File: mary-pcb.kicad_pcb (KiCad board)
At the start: 2 copper layers, 69 parts, among them SW1 SW_Push, SW2 Rotary_Encoder_Switch, U1 ATmega32U4-AU, Y1 16MHz

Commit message: place switches on pcb
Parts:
- moved MX20 236.5 mm to (257.2, 114.3)
- moved MX26 235.3 mm to (257.2, 123.8), turned to 90 degrees
- moved MX16 230.2 mm to (257.2, 85.7), turned to 90 degrees
- moved MX25 216.6 mm to (257.2, 133.3)
- moved MX23 199.1 mm to (219.1, 133.3)
- moved MX24 176.6 mm to (238.1, 133.3)
- moved MX3 175.1 mm to (238.1, 33.3)
- moved MX21 173.2 mm to (209.6, 133.3)
- moved MX15 171.3 mm to (257.2, 95.2)
- moved MX22 168.2 mm to (200.0, 133.3)
- moved MX6 152.2 mm to (238.1, 57.1)
- moved MX1 135.7 mm to (200.0, 33.3)
- moved MX14 135.2 mm to (238.1, 95.2)
- moved MX19 134.9 mm to (238.1, 114.3)
- moved MX8 134.4 mm to (200.0, 76.2)
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
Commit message: tentative rotary encoder placement
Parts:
- moved SW2 121.4 mm to (257.2, 33.3)
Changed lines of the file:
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@@
   )
   (module Keebio-Parts:RotaryEncoder_EC11 (layer F.Cu)
-    (at 146.2075 82.59125)
+    (at 257.175 33.3375)
     (descr "Alps rotary encoder, EC12E... with switch, vertical shaft, http://www.alps.com/prod/info/E/HTML/Encoder/Incremental/EC11/EC11E15204A3.html")
     (tags "rotary encoder")

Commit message: fix switch placement
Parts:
- moved MX1 4.76 mm to (200.0, 28.6)
- moved MX2 4.76 mm to (219.1, 28.6)
- moved MX3 4.76 mm to (238.1, 28.6)
- moved SW2 4.76 mm to (257.2, 28.6), turned to 90 degrees
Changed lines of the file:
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@@
   )
   (module Keebio-Parts:RotaryEncoder_EC11 (layer F.Cu)
-    (at 257.175 33.3375)
+    (at 257.175 28.575 90)
     (descr "Alps rotary encoder, EC12E... with switch, vertical shaft, http://www.alps.com/prod/info/E/HTML/Encoder/Incremental/EC11/EC11E15204A3.html")
     (tags "rotary encoder")
-    (fp_text reference SW2 (at -4.7 -7.2) (layer F.Fab)
-      (effects (font (size 1 1) (thickness 0.15)))
-    )
-    (fp_text value Rotary_Encoder_Switch (at 0 7.9) (layer F.Fab)
-      (effects (font (size 1 1) (thickness 0.15)))
-    )
-    (fp_text user %R (at 3.6 3.8) (layer F.Fab)
+    (fp_text reference SW2 (at -4.7 -7.2 90) (layer F.Fab)
+      (effects (font (size 1 1) (thickness 0.15)))
+    )
+    (fp_text value Rotary_Encoder_Switch (at 0 7.9 90) (layer F.Fab)
+      (effects (font (size 1 1) (thickness 0.15)))
+    )
+    (fp_text user %R (at 3.6 3.8 90) (layer F.Fab)
       (effects (font (size 1 1) (thickness 0.15)))
     )
@@
     (fp_circle (center 0 0) (end 3 0) (layer F.SilkS) (width 0.12))
     (fp_circle (center 0 0) (end 3 0) (layer F.Fab) (width 0.12))
-    (pad A thru_hole rect (at -7.5 -2.5) (size 2 2) (drill 1) (layers *.Cu *.Mask)
+    (pad A thru_hole rect (at -7.5 -2.5 90) (size 2 2) (drill 1) (layers *.Cu *.Mask)
       (net 49 "A(Left?)"))
-    (pad C thru_hole circle (at -7.5 0) (size 2 2) (drill 1) (layers *.Cu *.Mask)
+    (pad C thru_hole circle (at -7.5 0 90) (size 2 2) (drill 1) (layers *.Cu *.Mask)
       (net 1 GND))
-    (pad B thru_hole circle (at -7.5 2.5) (size 2 2) (drill 1) (layers *.Cu *.Mask)
+    (pad B thru_hole circle (at -7.5 2.5 90) (size 2 2) (drill 1) (layers *.Cu *.Mask)
       (net 50 "B(Right?)"))
-    (pad "" np_thru_hole rect (at 0 -5.6) (size 3.2 2) (drill oval 2.8 1.5) (layers *.Cu *.Mask))
-    (pad "" np_thru_hole rect (at 0 5.6) (size 3.2 2) (drill oval 2.8 1.5) (layers *.Cu *.Mask))
-    (pad S2 thru_hole circle (at 7 -2.5) (size 2 2) (drill 1) (layers *.Cu *.Mask)
+    (pad "" np_thru_hole rect (at 0 -5.6 90) (size 3.2 2) (drill oval 2.8 1.5) (layers *.Cu *.Mask))
+    (pad "" np_thru_hole rect (at 0 5.6 90) (size 3.2 2) (drill oval 2.8 1.5) (layers *.Cu *.Mask))
+    (pad S2 thru_hole circle (at 7 -2.5 90) (size 2 2) (drill 1) (layers *.Cu *.Mask)
       (net 10 "Net-(D4-Pad2)"))
-    (pad S1 thru_hole circle (at 7 2.5) (size 2 2) (drill 1) (layers *.Cu *.Mask)
+    (pad S1 thru_hole circle (at 7 2.5 90) (size 2 2) (drill 1) (layers *.Cu *.Mask)
       (net 40 Col3))
     (model ${KISYS3DMOD}/Rotary_Encoder.3dshapes/RotaryEncoder_Alps_EC11E-Switch_Vertical_H20mm.wrl
@@
   )
   (module MX_Alps_Hybrid:MX-1U-NoLED (layer F.Cu)
-    (at 238.125 33.3375)
+    (at 238.125 28.575)
     (fp_text reference MX3 (at 0 3.175) (layer Dwgs.User)
       (effects (font (size 1 1) (thickness 0.15)))
@@
   )
   (module MX_Alps_Hybrid:MX-1U-NoLED (layer F.Cu)
-    (at 219.075 33.3375)
+    (at 219.075 28.575)
     (fp_text reference MX2 (at 0 3.175) (layer Dwgs.User)
       (effects (font (size 1 1) (thickness 0.15)))
@@
   )
   (module MX_Alps_Hybrid:MX-1U-NoLED (layer F.Cu)
-    (at 200.025 33.3375)
+    (at 200.025 28.575)
     (fp_text reference MX1 (at 0 3.175) (layer Dwgs.User)
       (effects (font (size 1 1) (thickness 0.15)))

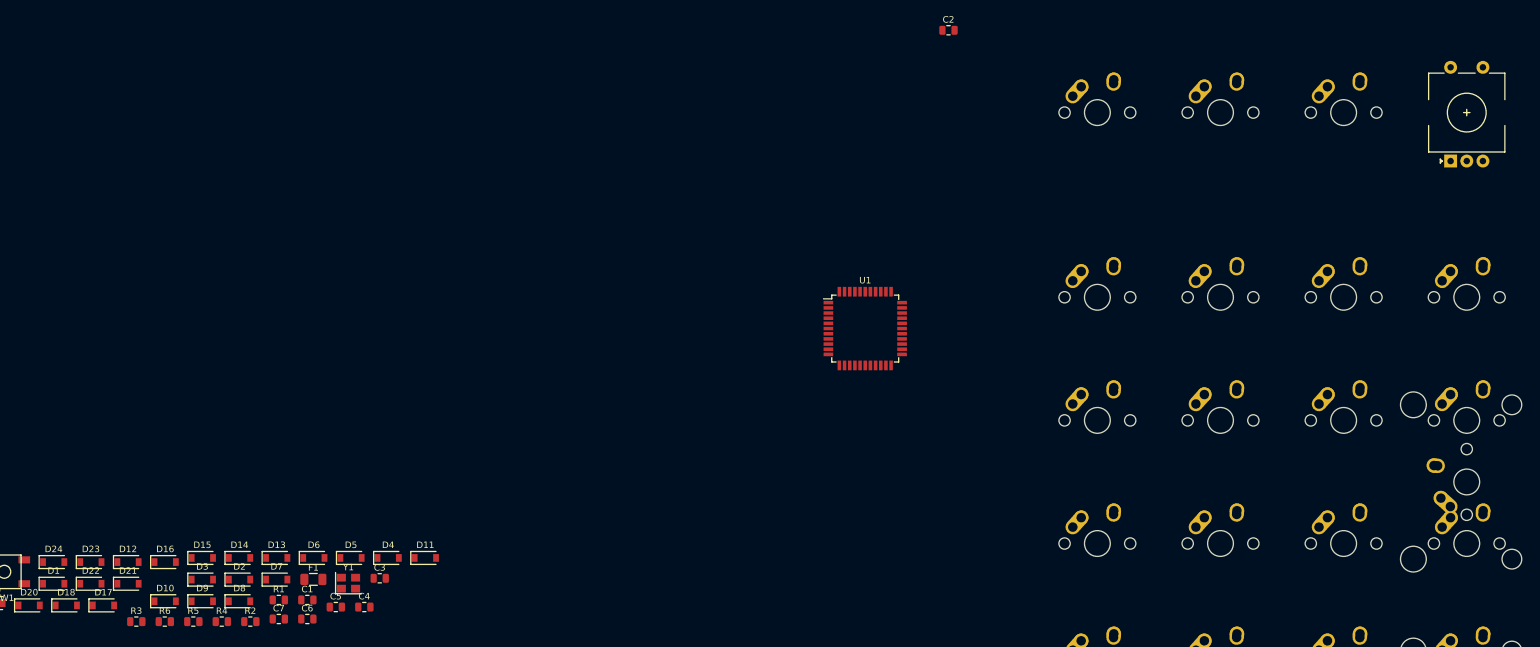
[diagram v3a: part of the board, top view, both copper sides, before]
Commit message: update pcb footprints, place diodes
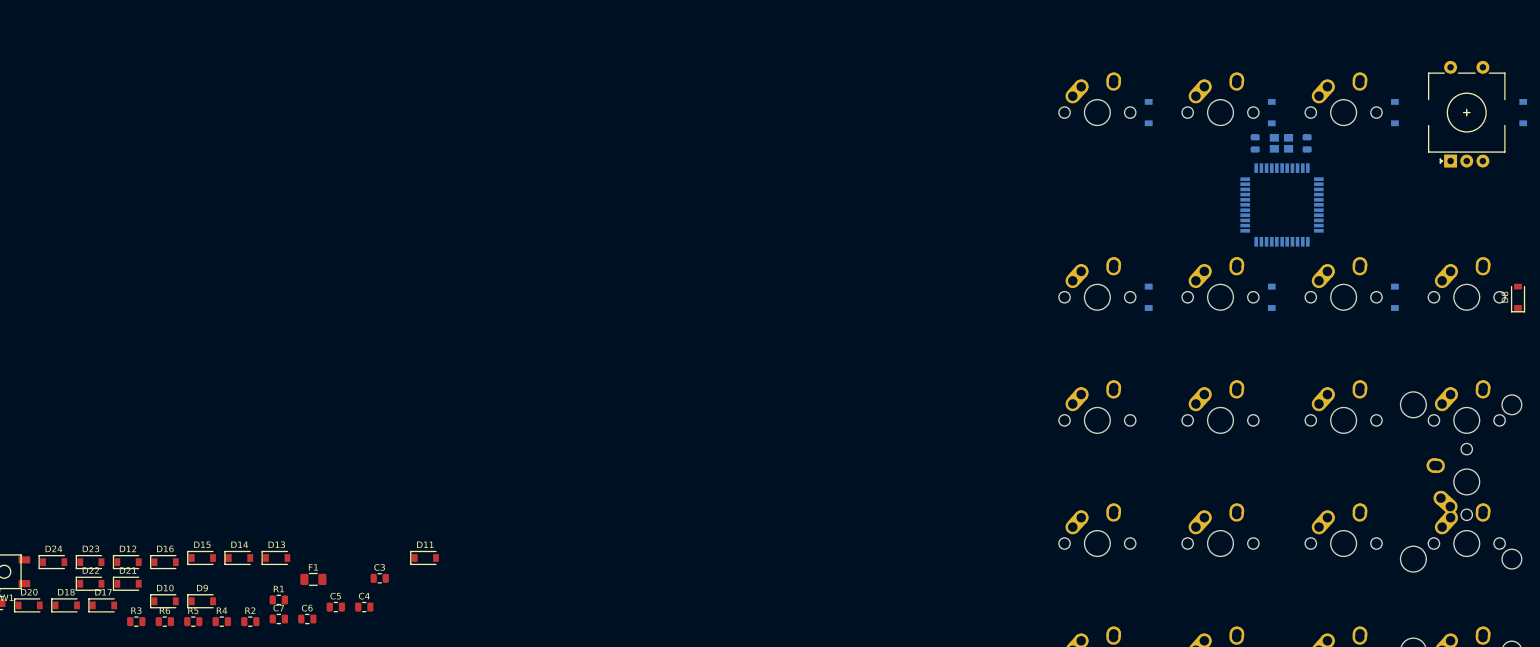
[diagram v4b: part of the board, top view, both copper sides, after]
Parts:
- C1, C2, D1, D2, D3, D4, D5, D6, D7, U1, Y1: moved to B.Cu
- moved D8 203.3 mm to (265.1, 57.1), turned to 90 degrees
- moved D3 198.2 mm to (246.1, 28.6), turned to 90 degrees
- moved D4 188.6 mm to (265.9, 28.6), turned to 90 degrees
- moved D1 184.4 mm to (208.0, 28.6), turned to 90 degrees
- moved D7 178.4 mm to (246.1, 57.1), turned to 90 degrees
- moved D2 175.3 mm to (227.0, 28.6), turned to 90 degrees
- moved C1 170.1 mm to (232.5, 33.3), turned to 90 degrees
- moved Y1 159.6 mm to (228.5, 33.3), turned to 180 degrees
- moved D6 153.6 mm to (227.0, 57.1), turned to 90 degrees
- moved D5 129.8 mm to (208.0, 57.1), turned to 90 degrees
- moved U1 67.3 mm to (228.6, 42.9)
- moved C2 50.6 mm to (224.4, 33.3), turned to 270 degrees
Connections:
- U1 pad 18: Row5 -> Net-(U1-Pad18)
- U1 pad 19: Col0 -> Net-(U1-Pad19)
- U1 pad 20: Col1 -> Net-(U1-Pad20)
- U1 pad 21: Col2 -> Net-(U1-Pad21)
- U1 pad 22: A(Left?) -> Net-(U1-Pad22)
- U1 pad 25: Col3 -> Net-(U1-Pad25)
- U1 pad 26: B(Right?) -> Net-(U1-Pad26)
- U1 pad 28: Row0 -> Net-(U1-Pad28)
- U1 pad 29: Row1 -> Net-(U1-Pad29)
- U1 pad 30: Row2 -> Net-(U1-Pad30)
- U1 pad 31: Row3 -> Net-(U1-Pad31)
- U1 pad 32: Row4 -> Net-(U1-Pad32)

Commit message: place resistors, diodes, reset, capacitors
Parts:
- C3, C4, C5, C6, C7, D10, D11, D12, D13, D14, D15, D16, D17, D18, D19, D20, D21, D22, D23, D24, D8, D9, F1, R1, R2, R3, R4, R5, R6, USB1: moved to B.Cu
- moved D20 156.6 mm to (188.9, 132.6), turned to 90 degrees
- moved D24 156.4 mm to (184.9, 153.2)
- moved USB1 151.9 mm to (153.2, 30.9)
- moved D19 146.0 mm to (172.2, 132.6), turned to 90 degrees
- moved D12 138.9 mm to (188.9, 94.5), turned to 90 degrees
- moved D23 135.7 mm to (168.3, 153.2)
- moved D16 134.5 mm to (188.9, 117.5), turned to 90 degrees
- moved D22 120.6 mm to (153.2, 153.2)
- moved D18 116.1 mm to (153.2, 132.6), turned to 90 degrees
- moved R6 115.8 mm to (161.9, 61.2), turned to 90 degrees
- moved R5 112.6 mm to (151.9, 42.0), turned to 90 degrees
- moved D15 112.5 mm to (172.2, 117.5), turned to 90 degrees
- moved R4 111.1 mm to (154.4, 42.0), turned to 90 degrees
- moved R3 110.1 mm to (135.4, 36.2), turned to 90 degrees
- moved SW1 103.2 mm to (124.6, 56.4)
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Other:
- board outline added: 76.2 x 123.8 mm

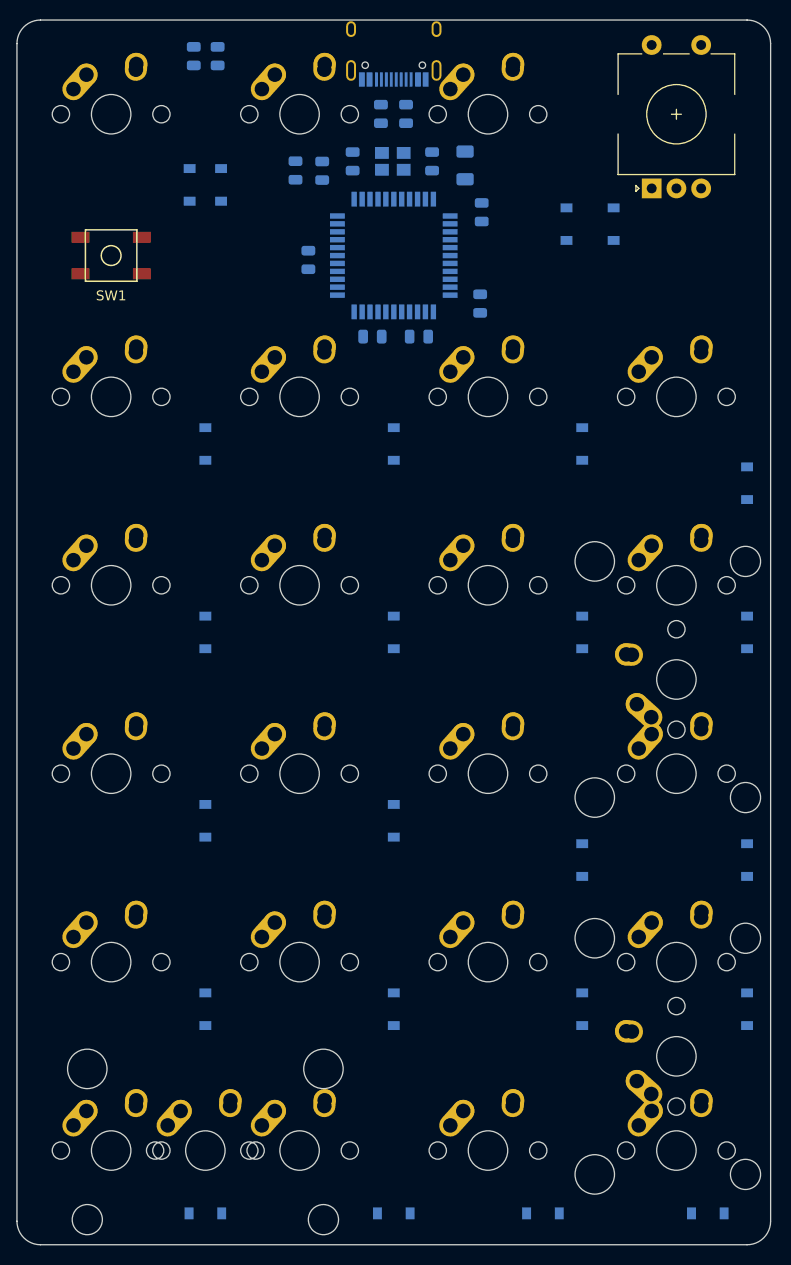
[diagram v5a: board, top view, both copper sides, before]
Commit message: complete routing
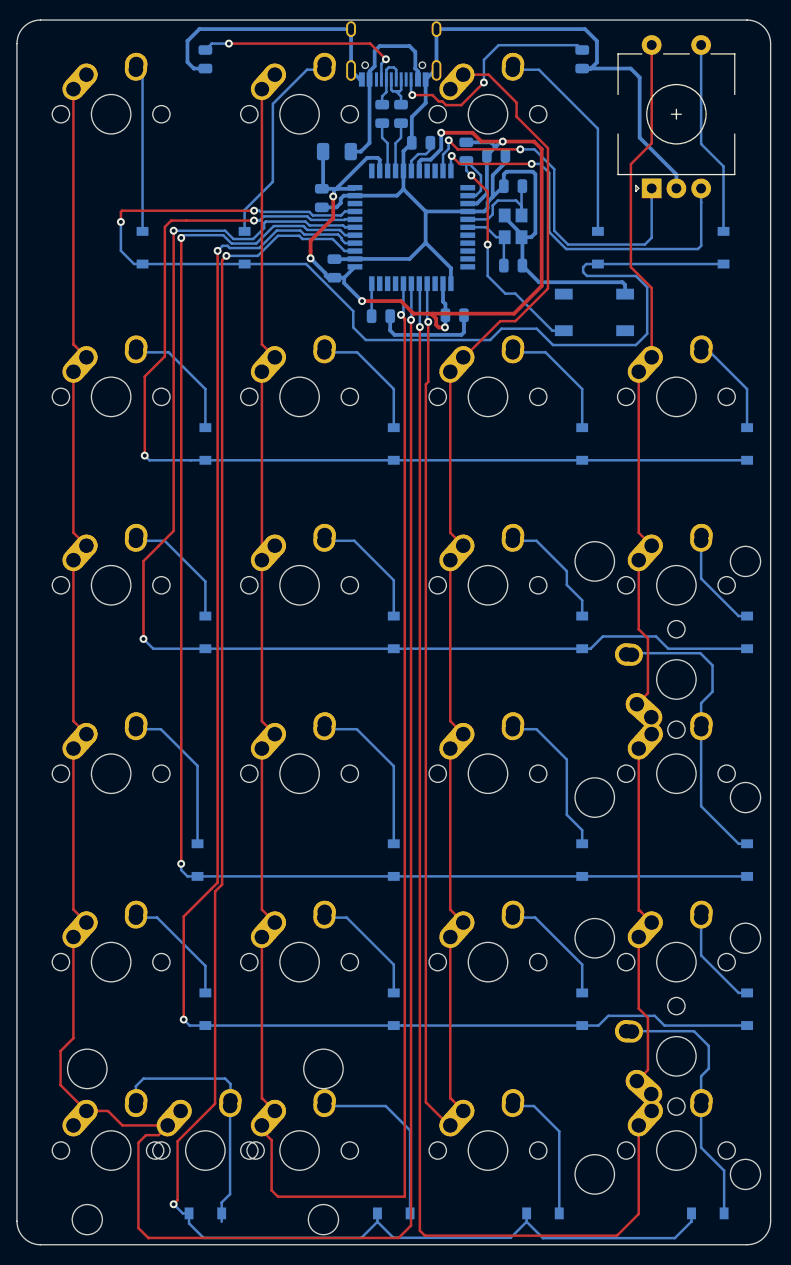
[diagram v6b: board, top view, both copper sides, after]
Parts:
- SW1: moved to B.Cu
- moved SW1 49.2 mm to (173.5, 62.1)
- moved R3 36.9 mm to (172.2, 36.5)
- moved C5 17.7 mm to (163.5, 46.3), turned to 0 degrees
- moved R1 17.4 mm to (160.5, 45.8)
- moved C3 16.4 mm to (156.0, 45.0), turned to 180 degrees
- moved C2 16.4 mm to (165.3, 49.3), turned to 180 degrees
- moved C7 14.9 mm to (145.9, 50.5), turned to 270 degrees
- moved Y1 13.8 mm to (165.3, 53.4), turned to 90 degrees
- moved C1 13.3 mm to (165.3, 57.4), turned to 0 degrees
- moved F1 13.0 mm to (147.4, 45.8), turned to 0 degrees
- moved D4 11.4 mm to (186.5, 55.6)
- moved C4 11.0 mm to (147.2, 57.7), turned to 90 degrees
- moved C6 10.8 mm to (159.4, 62.4), turned to 0 degrees
- moved R6 10.1 mm to (151.9, 62.5), turned to 180 degrees
- moved D1 7.94 mm to (127.8, 55.6)
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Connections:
- SW2 pad S1: Col3 -> Net-(D4-Pad2)
- SW2 pad S2: Net-(D4-Pad2) -> Col3
- U1 pad 10: Net-(U1-Pad10) -> A(Left?)
- U1 pad 11: Net-(U1-Pad11) -> B(Right?)
- U1 pad 26: Net-(U1-Pad26) -> Col2
- U1 pad 27: Net-(U1-Pad27) -> Col3
- U1 pad 28: Net-(U1-Pad28) -> Col0
- U1 pad 29: Net-(U1-Pad29) -> Col1
- U1 pad 36: Net-(U1-Pad36) -> Row5
- U1 pad 37: Net-(U1-Pad37) -> Row4
- U1 pad 38: Net-(U1-Pad38) -> Row3
- U1 pad 39: Net-(U1-Pad39) -> Row2
- U1 pad 40: Net-(U1-Pad40) -> Row1
- U1 pad 41: Net-(U1-Pad41) -> Row0
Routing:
- net Col0: track 0.00 -> 246.5 mm, vias 0 -> 1
- net Col3: track 0.00 -> 228.4 mm, vias 0 -> 1
- net Col1: track 0.00 -> 214.6 mm, vias 0 -> 1
- net Col2: track 0.00 -> 200.0 mm, vias 0 -> 1
- net Row5: track 0.00 -> 172.9 mm, vias 0 -> 2
- net GND: track 0.00 -> 169.9 mm
- net Row4: track 0.00 -> 152.7 mm, vias 0 -> 2
- net Row3: track 0.00 -> 140.5 mm, vias 0 -> 2
- net Row2: track 0.00 -> 124.9 mm, vias 0 -> 2
- net Row0: track 0.00 -> 114.2 mm, vias 0 -> 2
- net Row1: track 0.00 -> 104.9 mm, vias 0 -> 2
- net +5V: track 0.00 -> 99.6 mm, vias 0 -> 6
- net B(Right?): track 0.00 -> 40.1 mm, vias 0 -> 2
- net A(Left?): track 0.00 -> 37.1 mm, vias 0 -> 2
- net Net-(D16-Pad2): track 0.00 -> 29.7 mm
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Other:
- net class Default: trace_width 0.25 -> 0.254
- net class power added: clearance 0.2, trace_width 0.381, via_dia 0.8, via_drill 0.4

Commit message: complete routing, upload renders
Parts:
- moved SW1 11.3 mm to (182.9, 55.9)
- moved D3 4.72 mm to (170.7, 59.1)
- moved D2 4.23 mm to (135.7, 59.1)
- moved D4 4.23 mm to (188.9, 59.1)
- moved D1 3.49 mm to (127.8, 59.1)
- moved C5 3.46 mm to (167.0, 46.1)
- moved D21 3.13 mm to (136.8, 151.5), turned to 90 degrees
- moved C4 2.41 mm to (144.8, 57.7)
- moved D23 2.27 mm to (169.8, 151.5), turned to 90 degrees
- moved D22 1.69 mm to (153.0, 151.5), turned to 90 degrees
- moved D24 1.68 mm to (184.9, 151.5), turned to 90 degrees
- moved F1 1.54 mm to (145.9, 46.1)
- moved C7 1.53 mm to (144.5, 49.9)
- moved C2 1.24 mm to (165.9, 50.4)
- moved C6 0.86 mm to (158.5, 62.4)
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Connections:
- U1 pad 10: A(Left?) -> Net-(U1-Pad10)
- U1 pad 11: B(Right?) -> Net-(U1-Pad11)
- U1 pad 21: Net-(U1-Pad21) -> A(Left?)
- U1 pad 22: Net-(U1-Pad22) -> B(Right?)
- U1 pad 36: Row5 -> Row0
- U1 pad 37: Row4 -> Row1
- U1 pad 38: Row3 -> Row2
- U1 pad 39: Row2 -> Row3
- U1 pad 40: Row1 -> Row4
- U1 pad 41: Row0 -> Row5
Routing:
- net Row4: track 152.7 -> 187.3 mm, vias 2 -> 0
- net Row5: track 172.9 -> 202.7 mm, vias 2 -> 0
- net Row3: track 140.5 -> 169.0 mm, vias 2 -> 0
- net Row2: track 124.9 -> 145.2 mm, vias 2 -> 0
- net Row0: track 114.2 -> 95.9 mm
- net Row1: track 104.9 -> 123.2 mm, vias 2 -> 0
- net Col1: track 214.6 -> 202.7 mm
- net Col2: track 200.0 -> 188.8 mm
- net Net-(D2-Pad2): track 20.7 -> 30.4 mm, vias 0 -> 2
- net +5V: track 99.6 -> 108.7 mm, vias 6 -> 5
- net Col0: track 246.5 -> 237.6 mm
- net A(Left?): track 37.1 -> 30.6 mm
- net Net-(D4-Pad2): track 19.8 -> 26.2 mm
- net Net-(D22-Pad2): track 18.1 -> 12.9 mm
- net GND: track 169.9 -> 175.0 mm, vias 0 -> 6
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- added copper zone on B.Cu, net GND

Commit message: move usb
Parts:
- moved USB1 6.60 mm to (153.2, 24.3)
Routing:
- net GND: track 175.0 -> 187.3 mm
- net VCC: track 17.5 -> 24.1 mm
- net D-: track 6.13 -> 12.7 mm
- net D+: track 5.01 -> 11.6 mm
- net Net-(R3-Pad2): track 22.9 -> 19.7 mm
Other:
- board size 76.2 x 123.8 mm -> 76.2 x 130.8 mm
